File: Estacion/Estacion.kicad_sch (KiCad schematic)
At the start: 7 parts, among them U1 FN-M16P, U2 RP2040-ZERO, U3 DHT22

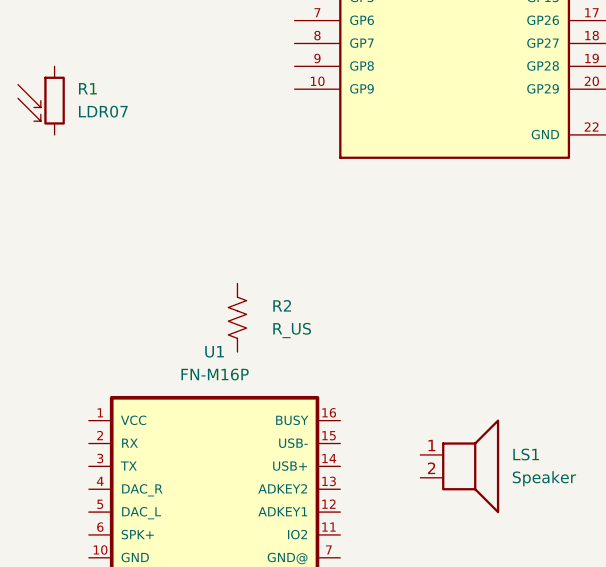
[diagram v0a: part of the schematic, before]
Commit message: Asociar simbolos con huellas
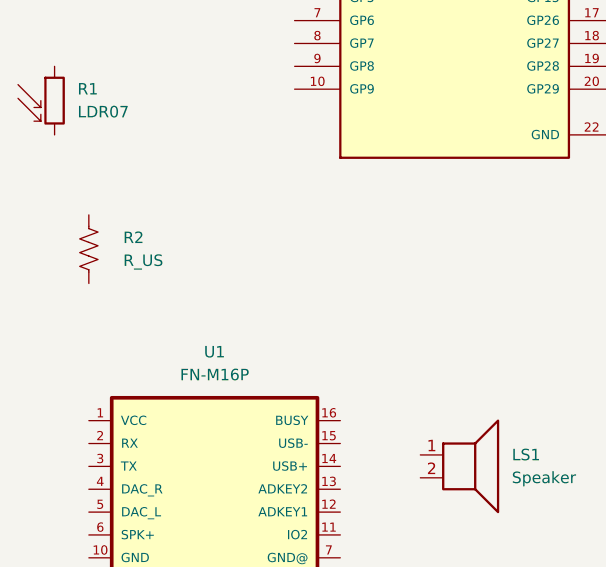
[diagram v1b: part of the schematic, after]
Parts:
- R2: footprint (none) -> Resistor_THT:R_Axial_DIN0204_L3.6mm_D1.6mm_P5.08mm_Horizontal
- U1: footprint FN-M16P:FN-M16P -> especificos:FN-M16P
- U2: footprint RP2040-ZERO:MODULE_RP2040-ZERO -> especificos:MODULE_RP2040-ZERO
- U3: footprint DHT22:XDCR_DHT22 -> especificos:XDCR_DHT22
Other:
- moved on the sheet: R2
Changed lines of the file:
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@@
 			)
 		)
-		(property "Footprint" "FN-M16P:FN-M16P"
+		(property "Footprint" "especificos:FN-M16P"
 			(at 116.84 110.49 0)
 			(hide yes)
@@
 	(symbol
 		(lib_id "Device:R_US")
-		(at 120.65 91.44 0)
+		(at 104.14 83.82 0)
 		(unit 1)
 		(body_style 1)
@@
 		(fields_autoplaced yes)
 		(property "Reference" "R2"
-			(at 124.46 90.1699 0)
+			(at 107.95 82.5499 0)
 			(show_name no)
 			(do_not_autoplace no)
@@
 		)
 		(property "Value" "R_US"
-			(at 124.46 92.7099 0)
+			(at 107.95 85.0899 0)
 			(show_name no)
 			(do_not_autoplace no)
@@
 			)
 		)
-		(property "Footprint" ""
-			(at 121.666 91.694 90)
+		(property "Footprint" "Resistor_THT:R_Axial_DIN0204_L3.6mm_D1.6mm_P5.08mm_Horizontal"
+			(at 105.156 84.074 90)
 			(hide yes)
 			(show_name no)
@@
 		)
 		(property "Datasheet" ""
-			(at 120.65 91.44 0)
+			(at 104.14 83.82 0)
 			(hide yes)
 			(show_name no)
@@
 		)
 		(property "Description" "Resistor, US symbol"
-			(at 120.65 91.44 0)
+			(at 104.14 83.82 0)
 			(hide yes)
 			(show_name no)
@@
 			)
 		)
-		(property "Footprint" "DHT22:XDCR_DHT22"
+		(property "Footprint" "especificos:XDCR_DHT22"
 			(at 176.53 93.98 0)
 			(hide yes)
@@
 			)
 		)
-		(property "Footprint" "RP2040-ZERO:MODULE_RP2040-ZERO"
+		(property "Footprint" "especificos:MODULE_RP2040-ZERO"
 			(at 144.78 53.34 0)
 			(hide yes)

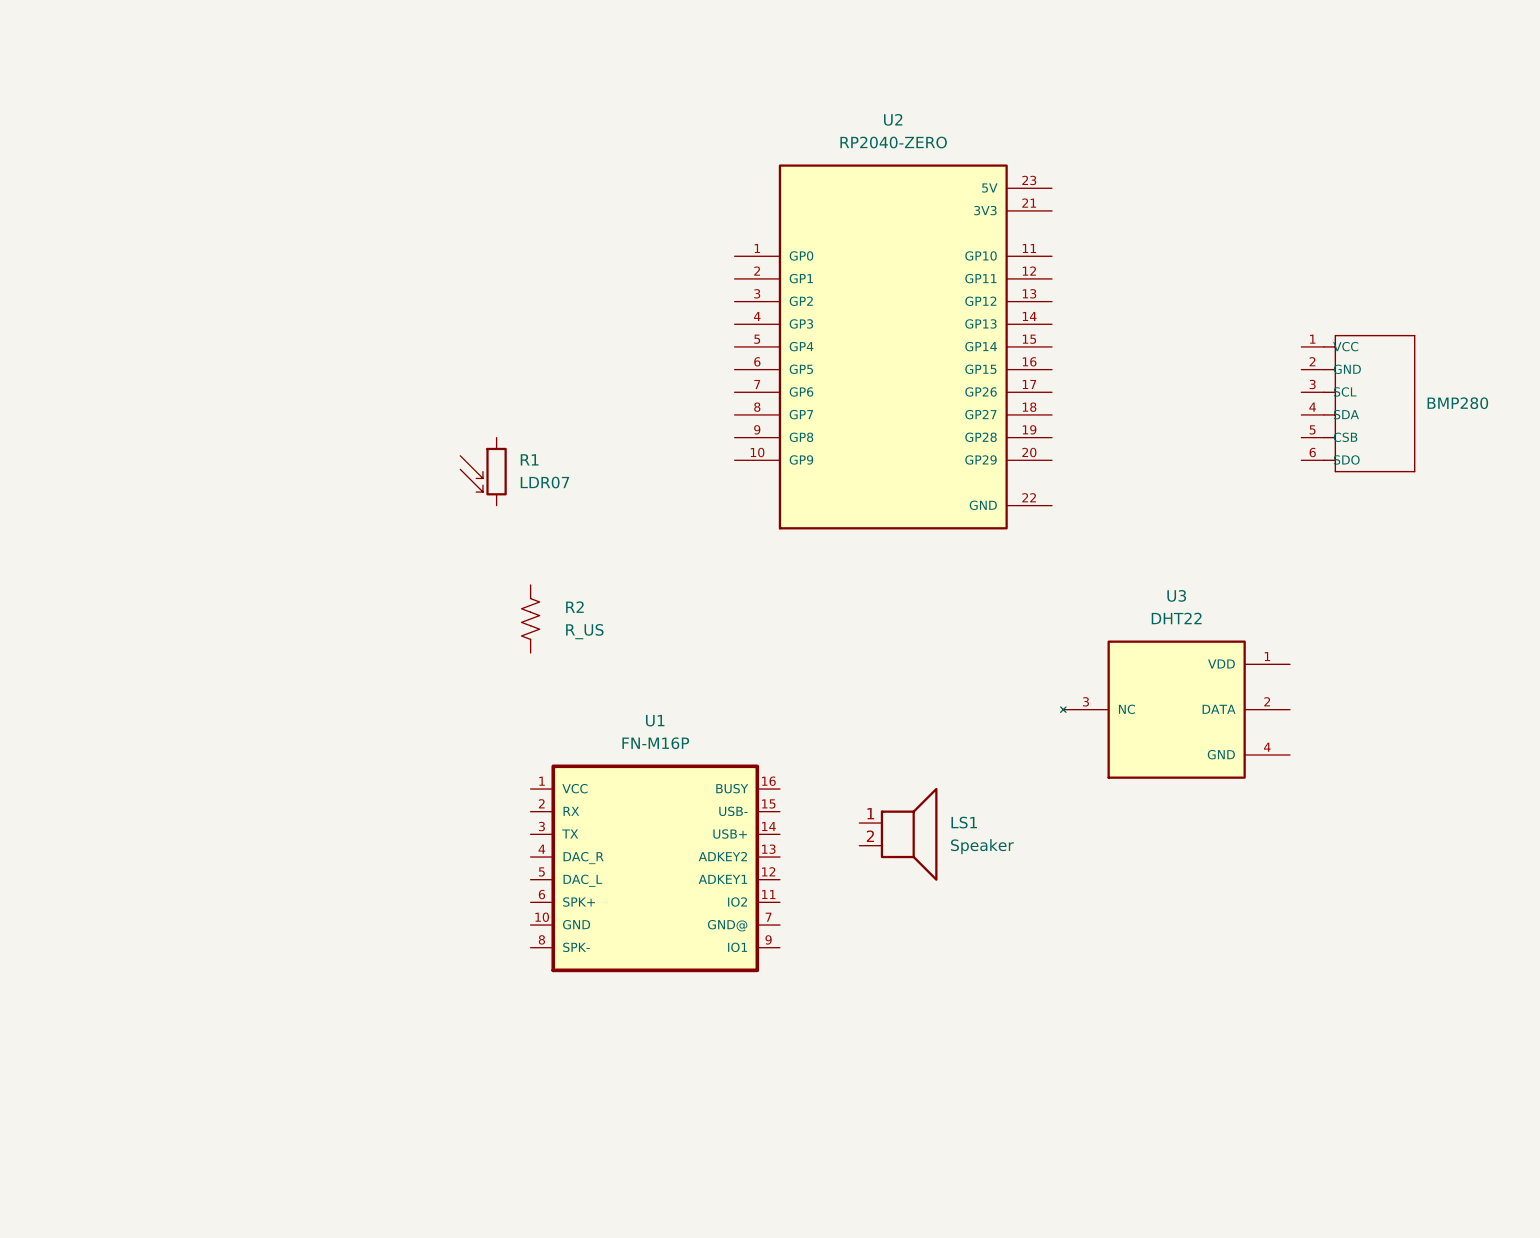
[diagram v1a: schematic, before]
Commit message: preparaciones
Relacionar footprints con modelados 3d, delimitar espacio de pcb, retocar conexiones y asegurar cumplimiento de ERC
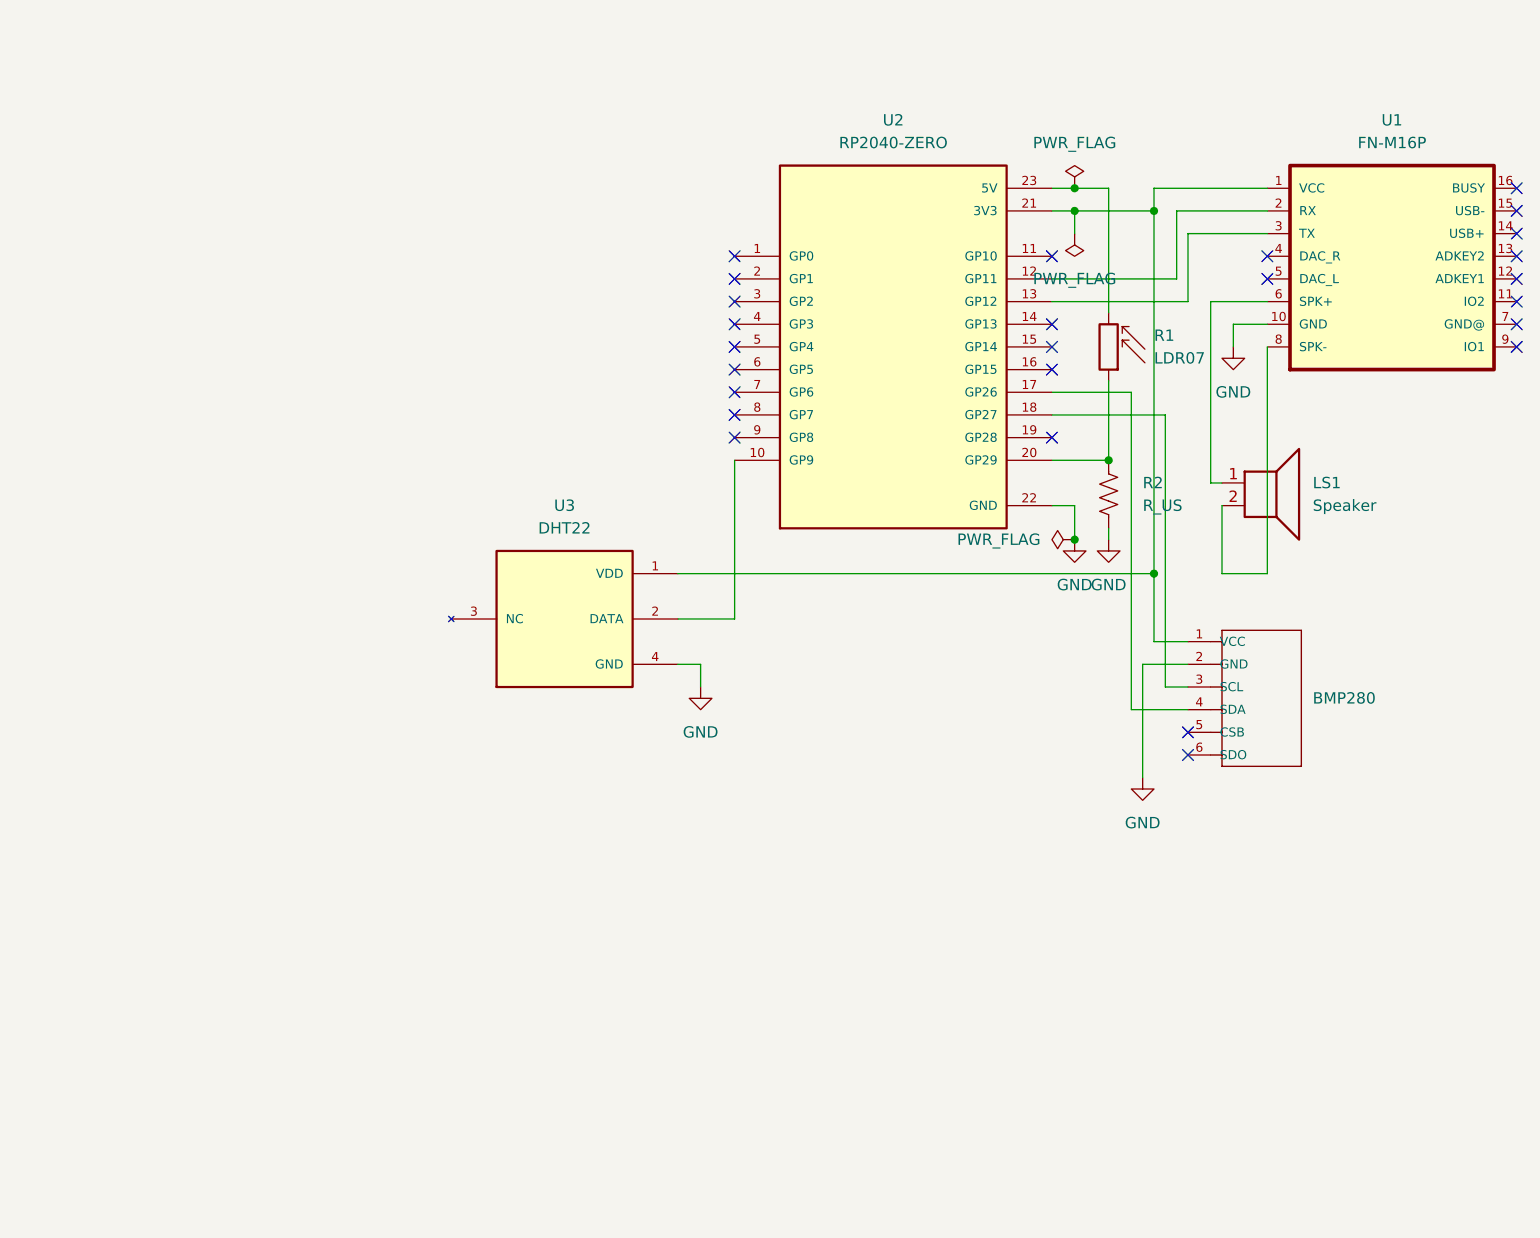
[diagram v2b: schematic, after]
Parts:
- BMP280: footprint PRESSURE-BMP180_LGA7_:LGA7-1.5-3.8X3.6MM -> especificos:BMP180
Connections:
- net at U1.1 (VCC): now also BMP280.1 (VCC), U2.21 (3V3), U3.1 (VDD)
- net GND: now reaches U1.10 (GND)
- net GND: now also BMP280.2 (GND), R2.2, U2.22 (GND), U3.4 (GND)
- net at U1.2 (RX): now also U2.12 (GP11)
- net at U1.3 (TX): now also U2.13 (GP12)
- net at U1.6 (SPK+): now also LS1.1
- net at U1.8 (SPK-): now also LS1.2
- net at R2.1: now also R1.1, U2.20 (GP29)
- net at U3.2 (DATA): now also U2.10 (GP9)
- net at R1.2: now also U2.23 (5V)
- net at U2.17 (GP26): now also BMP280.4 (SDA)
- net at U2.18 (GP27): now also BMP280.3 (SCL)
- no-connect marks 0 -> 26
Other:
- moved on the sheet: BMP280, LS1, R2, U1, U3

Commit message: ...
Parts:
- added D1: LED, symbol Device:LED
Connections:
- net GND: now also D1.1 (K)
- net at BMP280.1 (VCC), U1.1 (VCC), U2.21 (3V3)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: now also D1.2 (A)
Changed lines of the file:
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@@
+	)
+	(junction
+		(at 173.99 35.56)
+		(diameter 0)
+		(color 0 0 0 0)
 	)
 	(junction
@@
 	(wire
 		(pts
+			(xy 184.15 25.4) (xy 189.23 25.4)
+		)
+		(stroke
+			(width 0)
+			(type default)
+		)
+	)
+	(wire
+		(pts
 			(xy 165.1 38.1) (xy 165.1 40.64)
 		)
@@
 	(wire
 		(pts
+			(xy 173.99 25.4) (xy 173.99 35.56)
+		)
+		(stroke
+			(width 0)
+			(type default)
+		)
+	)
+	(wire
+		(pts
 			(xy 168.91 35.56) (xy 168.91 49.53)
+		)
+		(stroke
+			(width 0)
+			(type default)
+		)
+	)
+	(wire
+		(pts
+			(xy 176.53 25.4) (xy 173.99 25.4)
 		)
 		(stroke
@@
 		(in_pos_files yes)
 		(dnp no)
-		(fields_autoplaced yes)
 		(property "Reference" "R2"
-			(at 172.72 68.5799 0)
+			(at 165.354 68.326 0)
 			(show_name no)
 			(do_not_autoplace no)
@@
 		)
 		(property "Value" "R_US"
-			(at 172.72 71.1199 0)
+			(at 165.354 70.358 0)
 			(show_name no)
 			(do_not_autoplace no)
@@
 		(in_pos_files yes)
 		(dnp no)
-		(fields_autoplaced yes)
 		(property "Reference" "#FLG02"
 			(at 165.1 42.545 0)
@@
 		)
 		(property "Value" "PWR_FLAG"
-			(at 165.1 45.72 0)
+			(at 163.068 40.132 0)
 			(show_name no)
 			(do_not_autoplace no)
@@
 					(unit 1)
 				)
+			)
+		)
+	)
+	(symbol
+		(lib_id "Device:LED")
+		(at 180.34 25.4 180)
+		(unit 1)
+		(body_style 1)
+		(exclude_from_sim no)
+		(in_bom yes)
+		(on_board yes)
+		(in_pos_files yes)
+		(dnp no)
+		(fields_autoplaced yes)
+		(property "Reference" "D1"
+			(at 181.9275 17.78 0)
+			(show_name no)
+			(do_not_autoplace no)
+			(effects
+				(font
+					(size 1.27 1.27)
+				)
+			)
+		)
+		(property "Value" "LED"
+			(at 181.9275 20.32 0)
+			(show_name no)
+			(do_not_autoplace no)
+			(effects
+				(font
+					(size 1.27 1.27)
+				)
+			)
+		)
+		(property "Footprint" ""
+			(at 180.34 25.4 0)
+			(hide yes)
+			(show_name no)
+			(do_not_autoplace no)
+			(effects
+				(font
+					(size 1.27 1.27)
+				)
+			)
+		)
+		(property "Datasheet" ""
+			(at 180.34 25.4 0)
+			(hide yes)
+			(show_name no)
+			(do_not_autoplace no)
+			(effects
+				(font
+					(size 1.27 1.27)
+				)
+			)
+		)
+		(property "Description" "Light emitting diode"
+			(at 180.34 25.4 0)
+			(hide yes)
+			(show_name no)
+			(do_not_autoplace no)
+			(effects
+				(font
+					(size 1.27 1.27)
+				)
+			)
+		)
+		(property "Sim.Pins" "1=K 2=A"
+			(at 180.34 25.4 0)
+			(hide yes)
+			(show_name no)
+			(do_not_autoplace no)
+			(effects
+				(font
+					(size 1.27 1.27)
+				)
+			)
+		)
+		(pin "2"
+		)
+		(pin "1"
+		)
+		(instances
+			(project "Estacion"
+				(path "/65db9eb0-748a-4b13-b93f-b47348ad70f0"
+					(reference "D1")
+					(unit 1)
+				)
+			)
+		)
+	)
+	(symbol
+		(lib_id "power:GND")
+		(at 189.23 25.4 90)
+		(unit 1)
+		(body_style 1)
+		(exclude_from_sim no)
+		(in_bom yes)
+		(on_board yes)
+		(in_pos_files yes)
+		(dnp no)
+		(fields_autoplaced yes)
+		(property "Reference" "#PWR06"
+			(at 195.58 25.4 0)
+			(hide yes)
+			(show_name no)
+			(do_not_autoplace no)
+			(effects
+				(font
+					(size 1.27 1.27)
+				)
+			)
+		)
+		(property "Value" "GND"
+			(at 193.04 25.3999 90)
+			(show_name no)
+			(do_not_autoplace no)
+			(effects
+				(font
+					(size 1.27 1.27)
+				)
+				(justify right)
+			)
+		)
+		(property "Footprint" ""
+			(at 189.23 25.4 0)
+			(hide yes)
+			(show_name no)
+			(do_not_autoplace no)
+			(effects
+				(font
+					(size 1.27 1.27)
+				)
+			)
+		)
+		(property "Datasheet" ""
+			(at 189.23 25.4 0)
+			(hide yes)
+			(show_name no)
+			(do_not_autoplace no)
+			(effects
+				(font
+					(size 1.27 1.27)
+				)
+			)
+		)
+		(property "Description" "Power symbol creates a global label with name \"GND\" , ground"
+			(at 189.23 25.4 0)
+			(hide yes)
+			(show_name no)
+			(do_not_autoplace no)
+			(effects
+				(font
+					(size 1.27 1.27)
+				)
+			)
+		)
+		(pin "1"
+		)
+		(instances
+			(project "Estacion"
+				(path "/65db9eb0-748a-4b13-b93f-b47348ad70f0"
+					(reference "#PWR06")
+					(unit 1)
+				)
